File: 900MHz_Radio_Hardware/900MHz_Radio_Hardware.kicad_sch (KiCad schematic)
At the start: 10 parts, among them U1 TSR_1-2450

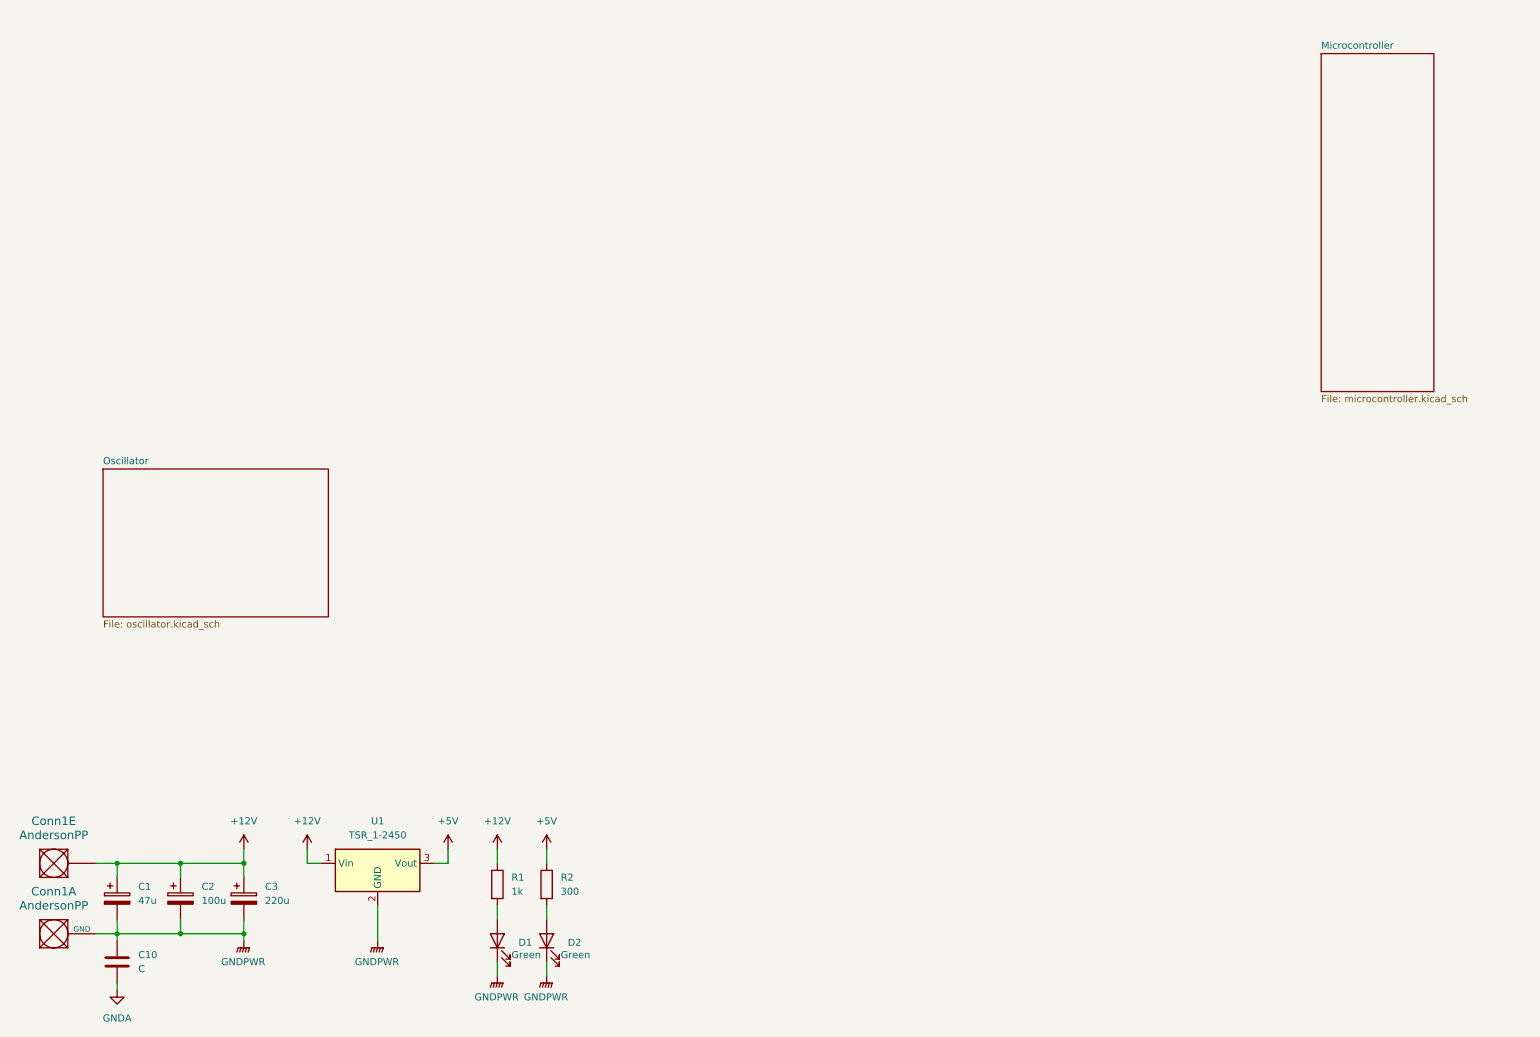
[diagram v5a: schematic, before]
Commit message: Completed oscillator
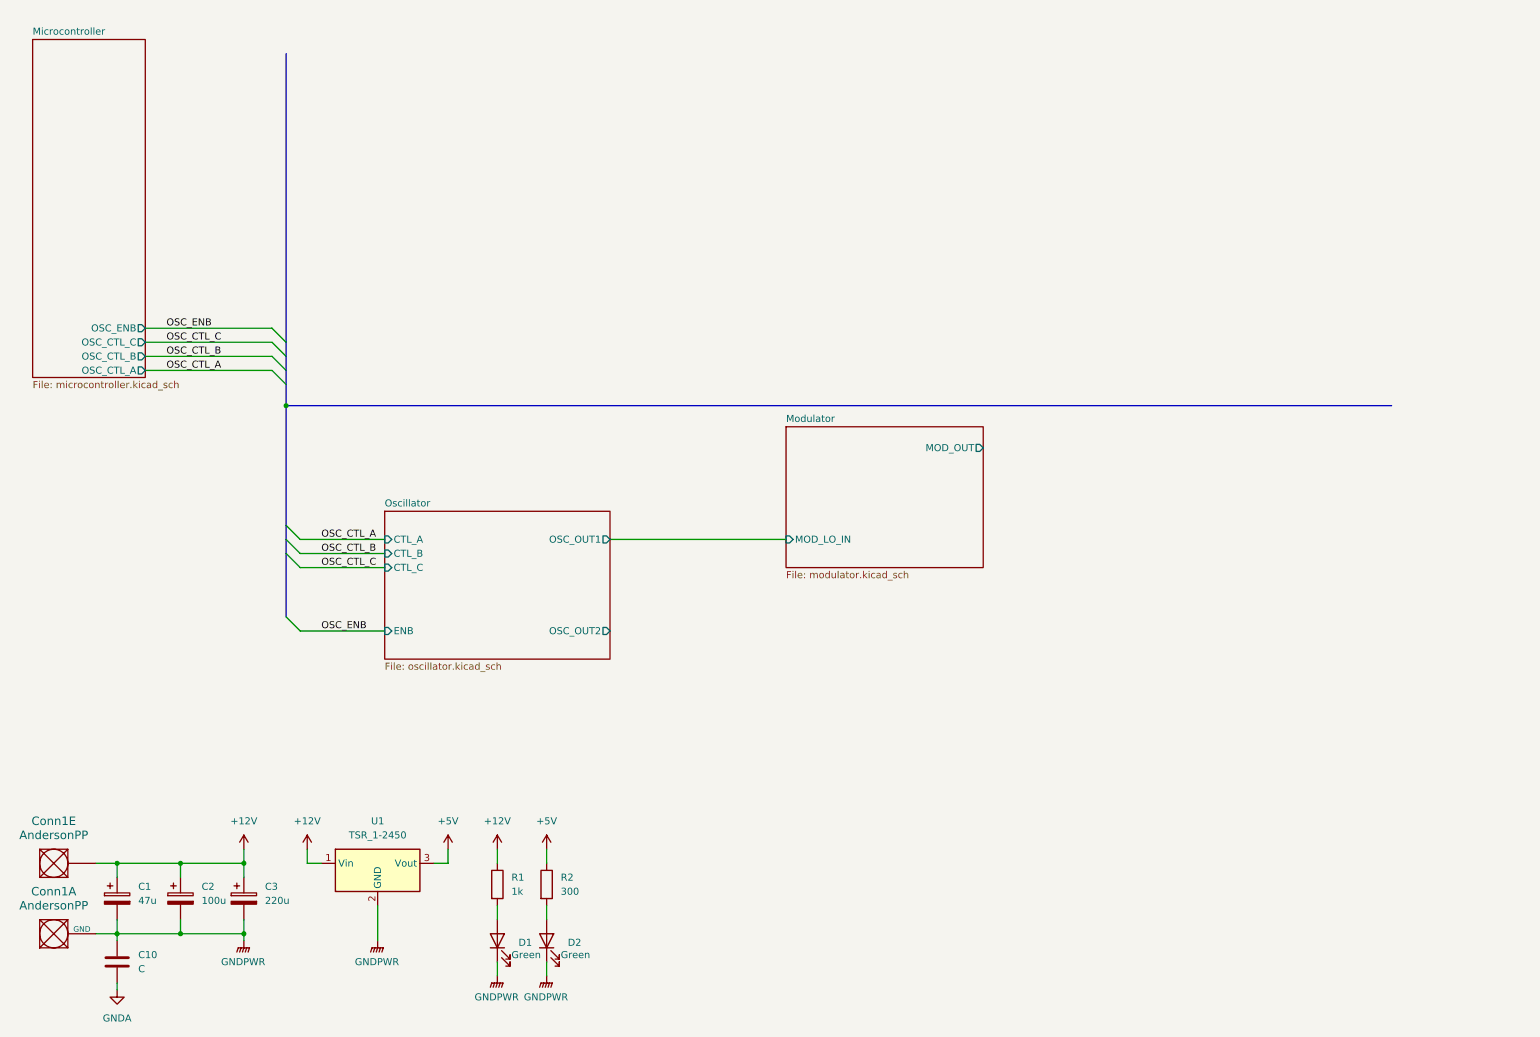
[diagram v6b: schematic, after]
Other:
- added sheet Modulator (modulator.kicad_sch)
- sheet Microcontroller ports: added OSC_CTL_A, OSC_CTL_B, OSC_CTL_C, OSC_ENB; removed none
- sheet Oscillator ports: added CTL_A, CTL_B, CTL_C, ENB, OSC_OUT1, OSC_OUT2; removed none
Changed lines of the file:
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@@
   (junction (at 30.48 180.34) (diameter 0) (color 0 0 0 0)
   )
+  (junction (at 60.96 85.09) (diameter 0) (color 0 0 0 0)
+  )
   (junction (at 41.91 180.34) (diameter 0) (color 0 0 0 0)
   )
@@
   (junction (at 53.34 180.34) (diameter 0) (color 0 0 0 0)
   )
+  (bus_entry (at 58.42 73.66) (size 2.54 2.54)
+    (stroke (width 0) (type default))
+  )
+  (bus_entry (at 58.42 71.12) (size 2.54 2.54)
+    (stroke (width 0) (type default))
+  )
+  (bus_entry (at 58.42 76.2) (size 2.54 2.54)
+    (stroke (width 0) (type default))
+  )
+  (bus_entry (at 60.96 109.22) (size 2.54 2.54)
+    (stroke (width 0) (type default))
+  )
+  (bus_entry (at 60.96 111.76) (size 2.54 2.54)
+    (stroke (width 0) (type default))
+  )
+  (bus_entry (at 58.42 78.74) (size 2.54 2.54)
+    (stroke (width 0) (type default))
+  )
+  (bus_entry (at 60.96 123.19) (size 2.54 2.54)
+    (stroke (width 0) (type default))
+  )
+  (bus_entry (at 60.96 106.68) (size 2.54 2.54)
+    (stroke (width 0) (type default))
+  )
   (wire (pts (xy 26.67 167.64) (xy 30.48 167.64))
     (stroke (width 0) (type default))
@@
     (stroke (width 0) (type default))
   )
+  (wire (pts (xy 63.5 109.22) (xy 78.74 109.22))
+    (stroke (width 0) (type default))
+  )
+  (bus (pts (xy 60.96 73.66) (xy 60.96 76.2))
+    (stroke (width 0) (type default))
+  )
   (wire (pts (xy 30.48 177.8) (xy 30.48 180.34))
     (stroke (width 0) (type default))
   )
+  (bus (pts (xy 60.96 21.59) (xy 60.96 73.66))
+    (stroke (width 0) (type default))
+  )
   (wire (pts (xy 90.17 165.1) (xy 90.17 167.64))
     (stroke (width 0) (type default))
   )
+  (bus (pts (xy 60.96 81.28) (xy 60.96 85.09))
+    (stroke (width 0) (type default))
+  )
   (wire (pts (xy 107.95 185.42) (xy 107.95 187.96))
     (stroke (width 0) (type default))
@@
     (stroke (width 0) (type default))
   )
+  (wire (pts (xy 63.5 111.76) (xy 78.74 111.76))
+    (stroke (width 0) (type default))
+  )
   (wire (pts (xy 30.48 180.34) (xy 41.91 180.34))
     (stroke (width 0) (type default))
@@
     (stroke (width 0) (type default))
   )
+  (wire (pts (xy 35.56 78.74) (xy 58.42 78.74))
+    (stroke (width 0) (type default))
+  )
+  (bus (pts (xy 60.96 109.22) (xy 60.96 111.76))
+    (stroke (width 0) (type default))
+  )
+  (bus (pts (xy 60.96 78.74) (xy 60.96 81.28))
+    (stroke (width 0) (type default))
+  )
   (wire (pts (xy 30.48 167.64) (xy 41.91 167.64))
     (stroke (width 0) (type default))
@@
     (stroke (width 0) (type default))
   )
+  (wire (pts (xy 63.5 114.3) (xy 78.74 114.3))
+    (stroke (width 0) (type default))
+  )
+  (wire (pts (xy 35.56 73.66) (xy 58.42 73.66))
+    (stroke (width 0) (type default))
+  )
+  (bus (pts (xy 60.96 85.09) (xy 260.35 85.09))
+    (stroke (width 0) (type default))
+  )
+  (bus (pts (xy 60.96 111.76) (xy 60.96 123.19))
+    (stroke (width 0) (type default))
+  )
   (wire (pts (xy 64.77 165.1) (xy 64.77 167.64))
     (stroke (width 0) (type default))
   )
+  (wire (pts (xy 63.5 125.73) (xy 78.74 125.73))
+    (stroke (width 0) (type default))
+  )
   (wire (pts (xy 30.48 189.23) (xy 30.48 190.5))
     (stroke (width 0) (type default))
@@
     (stroke (width 0) (type default))
   )
+  (wire (pts (xy 119.38 109.22) (xy 151.13 109.22))
+    (stroke (width 0) (type default))
+  )
+  (bus (pts (xy 60.96 76.2) (xy 60.96 78.74))
+    (stroke (width 0) (type default))
+  )
+  (wire (pts (xy 35.56 76.2) (xy 58.42 76.2))
+    (stroke (width 0) (type default))
+  )
+  (bus (pts (xy 60.96 85.09) (xy 60.96 106.68))
+    (stroke (width 0) (type default))
+  )
+  (bus (pts (xy 60.96 106.68) (xy 60.96 109.22))
+    (stroke (width 0) (type default))
+  )
   (wire (pts (xy 53.34 180.34) (xy 53.34 177.8))
     (stroke (width 0) (type default))
   )
+  (wire (pts (xy 35.56 71.12) (xy 58.42 71.12))
+    (stroke (width 0) (type default))
+  )
   (wire (pts (xy 41.91 180.34) (xy 53.34 180.34))
     (stroke (width 0) (type default))
@@
   (wire (pts (xy 26.67 180.34) (xy 30.48 180.34))
     (stroke (width 0) (type default))
+  )
+  (label "OSC_CTL_B" (at 39.37 76.2 0) (fields_autoplaced)
+    (effects (font (size 1.27 1.27)) (justify left bottom))
+  )
+  (label "OSC_CTL_B" (at 67.31 111.76 0) (fields_autoplaced)
+    (effects (font (size 1.27 1.27)) (justify left bottom))
+  )
+  (label "OSC_ENB" (at 67.31 125.73 0) (fields_autoplaced)
+    (effects (font (size 1.27 1.27)) (justify left bottom))
+  )
+  (label "OSC_CTL_A" (at 67.31 109.22 0) (fields_autoplaced)
+    (effects (font (size 1.27 1.27)) (justify left bottom))
+  )
+  (label "OSC_CTL_A" (at 39.37 78.74 0) (fields_autoplaced)
+    (effects (font (size 1.27 1.27)) (justify left bottom))
+  )
+  (label "OSC_CTL_C" (at 39.37 73.66 0) (fields_autoplaced)
+    (effects (font (size 1.27 1.27)) (justify left bottom))
+  )
+  (label "OSC_ENB" (at 39.37 71.12 0) (fields_autoplaced)
+    (effects (font (size 1.27 1.27)) (justify left bottom))
+  )
+  (label "OSC_CTL_C" (at 67.31 114.3 0) (fields_autoplaced)
+    (effects (font (size 1.27 1.27)) (justify left bottom))
   )
   (symbol (lib_id "Device:C_Polarized") (at 41.91 173.99 0) (unit 1)
@@
     )
   )
-  (sheet (at 27.94 96.52) (size 40.64 26.67) (fields_autoplaced)
+  (sheet (at 151.13 88.9) (size 35.56 25.4) (fields_autoplaced)
     (stroke (width 0.1524) (type solid))
     (fill (color 0 0 0 0.0000))
-    (property "Sheetname" "Oscillator" (at 27.94 95.8084 0)
+    (property "Sheetname" "Modulator" (at 151.13 88.1884 0)
       (effects (font (size 1.27 1.27)) (justify left bottom))
     )
-    (property "Sheetfile" "oscillator.kicad_sch" (at 27.94 123.7746 0)
+    (property "Sheetfile" "modulator.kicad_sch" (at 151.13 114.8846 0)
       (effects (font (size 1.27 1.27)) (justify left top))
     )
-    (instances
-      (project "900MHz_Radio_Hardware"
-        (path "/8d477a51-3dbb-4c04-84c7-90186d141eda" (page "3"))
-      )
-    )
-  )
-  (sheet (at 247.65 21.59) (size 20.32 60.96) (fields_autoplaced)
+    (pin "MOD_LO_IN" input (at 151.13 109.22 180)
+      (effects (font (size 1.27 1.27)) (justify left))
+    )
+    (pin "MOD_OUT" output (at 186.69 92.71 0)
+      (effects (font (size 1.27 1.27)) (justify right))
+    )
+    (instances
+      (project "900MHz_Radio_Hardware"
+        (path "/8d477a51-3dbb-4c04-84c7-90186d141eda" (page "4"))
+      )
+    )
+  )
+  (sheet (at 78.74 104.14) (size 40.64 26.67) (fields_autoplaced)
     (stroke (width 0.1524) (type solid))
     (fill (color 0 0 0 0.0000))
-    (property "Sheetname" "Microcontroller" (at 247.65 20.8784 0)
+    (property "Sheetname" "Oscillator" (at 78.74 103.4284 0)
       (effects (font (size 1.27 1.27)) (justify left bottom))
     )
-    (property "Sheetfile" "microcontroller.kicad_sch" (at 247.65 83.1346 0)
+    (property "Sheetfile" "oscillator.kicad_sch" (at 78.74 131.3946 0)
       (effects (font (size 1.27 1.27)) (justify left top))
     )
-    (instances
+    (pin "OSC_OUT1" output (at 119.38 109.22 0)
+      (effects (font (size 1.27 1.27)) (justify right))
+    )
+    (pin "OSC_OUT2" output (at 119.38 125.73 0)
+      (effects (font (size 1.27 1.27)) (justify right))
+    )
+    (pin "ENB" input (at 78.74 125.73 180)
+      (effects (font (size 1.27 1.27)) (justify left))
+    )
+    (pin "CTL_A" input (at 78.74 109.22 180)
+      (effects (font (size 1.27 1.27)) (justify left))
+    )
+    (pin "CTL_B" input (at 78.74 111.76 180)
+      (effects (font (size 1.27 1.27)) (justify left))
+    )
+    (pin "CTL_C" input (at 78.74 114.3 180)
+      (effects (font (size 1.27 1.27)) (justify left))
+    )
+    (instances
+      (project "900MHz_Radio_Hardware"
+        (path "/8d477a51-3dbb-4c04-84c7-90186d141eda" (page "3"))
+      )
+    )
+  )
+  (sheet (at 15.24 19.05) (size 20.32 60.96) (fields_autoplaced)
+    (stroke (width 0.1524) (type solid))
+    (fill (color 0 0 0 0.0000))
+    (property "Sheetname" "Microcontroller" (at 15.24 18.3384 0)
+      (effects (font (size 1.27 1.27)) (justify left bottom))
+    )
+    (property "Sheetfile" "microcontroller.kicad_sch" (at 15.24 80.5946 0)
+      (effects (font (size 1.27 1.27)) (justify left top))
+    )
+    (pin "OSC_CTL_A" output (at 35.56 78.74 0)
+      (effects (font (size 1.27 1.27)) (justify right))
+    )
+    (pin "OSC_CTL_B" output (at 35.56 76.2 0)
+      (effects (font (size 1.27 1.27)) (justify right))
+    )
+    (pin "OSC_CTL_C" output (at 35.56 73.66 0)
+      (effects (font (size 1.27 1.27)) (justify right))
+    )
+    (pin "OSC_ENB" output (at 35.56 71.12 0)
+      (effects (font (size 1.27 1.27)) (justify right))
+    )
+    (instances
